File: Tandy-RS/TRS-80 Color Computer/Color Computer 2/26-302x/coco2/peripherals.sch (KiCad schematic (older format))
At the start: 45 parts, among them J1 Left Joystick, J2 Right Joystick, J3 RS232, J4 Cassette, J5 Conn_01x16_Female, K1 HB1-DC5V-H62, Q1 2N3055, U1 SC77527P, U2 6821, U3 SC77526, U7 6822

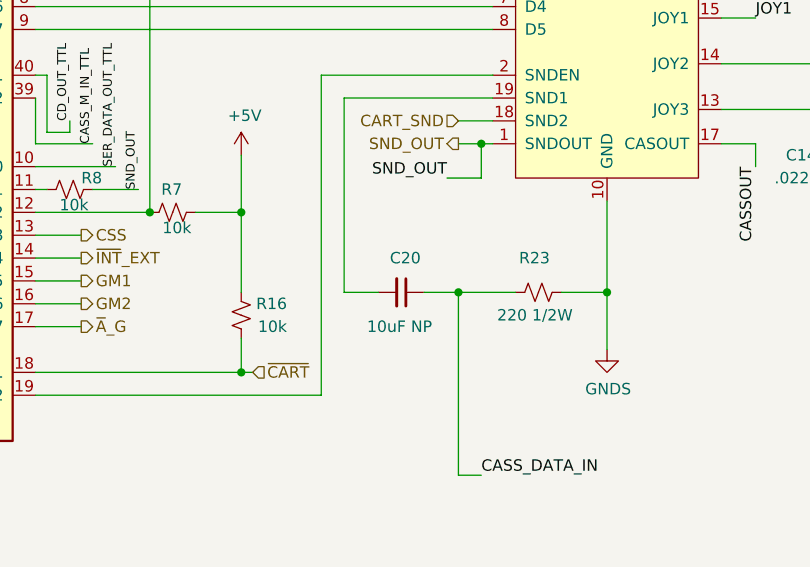
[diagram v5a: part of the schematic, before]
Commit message: Fixed some footprints that had wrong number of pins.
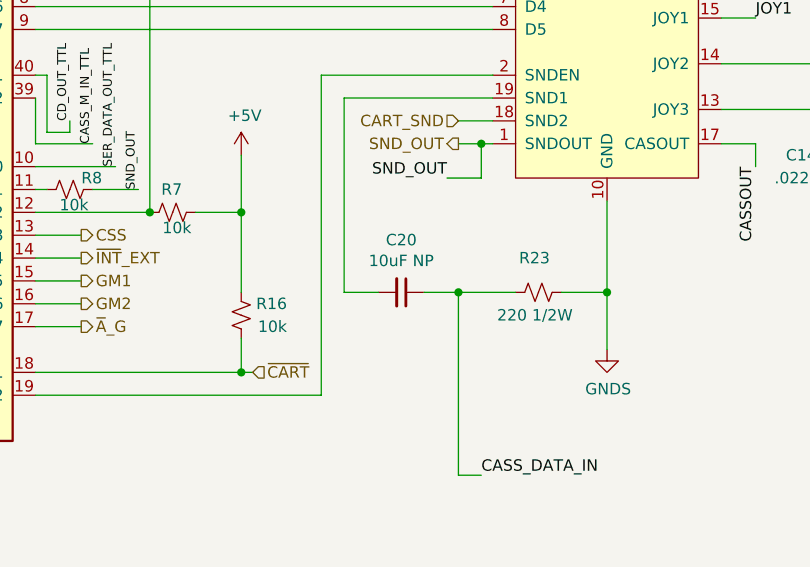
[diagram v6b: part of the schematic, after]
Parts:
- J5: footprint Connector_PinHeader_2.54mm:PinHeader_1x15_P2.54mm_Vertical -> Connector_PinHeader_2.54mm:PinHeader_1x16_P2.54mm_Vertical
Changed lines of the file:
@@
 F 0 "J5" H 5028 1826 50  0000 L CNN
 F 1 "Conn_01x16_Female" H 5028 1735 50  0000 L CNN
-F 2 "Connector_PinHeader_2.54mm:PinHeader_1x15_P2.54mm_Vertical" H 5000 1850 50  0001 C CNN
+F 2 "Connector_PinHeader_2.54mm:PinHeader_1x16_P2.54mm_Vertical" H 5000 1850 50  0001 C CNN
 F 3 "https://www.te.com/commerce/DocumentDelivery/DDEController?Action=srchrtrv&DocNm=520415&DocType=Customer+Drawing&DocLang=English" H 5000 1850 50  0001 C CNN
 F 4 "digikey" H 5000 1850 50  0001 C CNN "Vendor"
@@
 	5500 5900 5350 5900
 $Comp
-L Device:C_Small C20
-U 1 1 61067F63
-P 5100 6650
-F 0 "C20" V 4950 6600 50  0000 L CNN
-F 1 "10uF NP" V 5250 6500 50  0000 L CNN
-F 2 "Capacitor_THT:CP_Radial_D5.0mm_P2.50mm" H 5100 6650 50  0001 C CNN
-F 3 "http://nichicon-us.com/english/products/pdfs/e-ues.pdf" H 5100 6650 50  0001 C CNN
-F 4 "digikey" H 5100 6650 50  0001 C CNN "Vendor"
-F 5 "493-10824-1-ND" H 5100 6650 50  0001 C CNN "Vendor part#"
-F 6 "UES1E100MDM1TD" H 5100 6650 50  0001 C CNN "Manufacturer part#"
-	1    5100 6650
-	0    1    1    0
-$EndComp
-$Comp
 L Connector:DIN-4 J3
 U 1 1 61098034
@@
 Wire Wire Line
 	6300 550  6300 1850
+Connection ~ 10000 950
+$Comp
+L Device:C_Small C20
+U 1 1 605E886F
+P 5100 6650
+F 0 "C20" V 4871 6650 50  0000 C CNN
+F 1 "10uF NP" V 4962 6650 50  0000 C CNN
+F 2 "Capacitor_THT:CP_Radial_D5.0mm_P2.50mm" H 5100 6650 50  0001 C CNN
+F 3 "http://nichicon-us.com/english/products/pdfs/e-ues.pdf" H 5100 6650 50  0001 C CNN
+F 4 "digikey" V 5100 6650 50  0001 C CNN "Vendor"
+F 5 "493-10824-1-ND" V 5100 6650 50  0001 C CNN "Vendor part#"
+F 6 "UES1E100MDM1TD" V 5100 6650 50  0001 C CNN "Manufacturer part#"
+	1    5100 6650
+	0    1    1    0
+$EndComp
 Wire Bus Line
 	1000 1150 1000 5400
-Connection ~ 10000 950
 $EndSCHEMATC

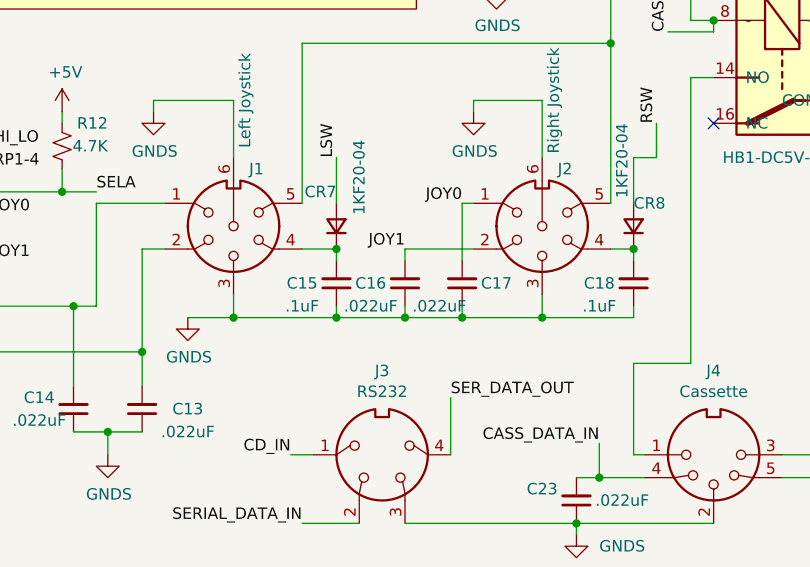
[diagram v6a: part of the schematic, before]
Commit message: -Finished PCB border -Placed components to match original board -added some 3D models for some components
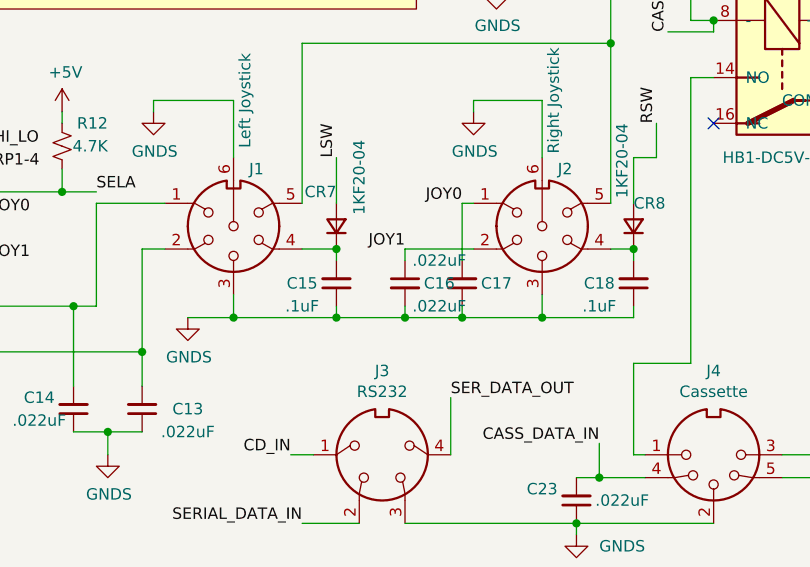
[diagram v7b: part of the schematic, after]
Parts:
- C13, C14, C16, C17, C22, C23: footprint Capacitor_THT:C_Disc_D8.0mm_W5.0mm_P5.00mm -> Capacitor_THT:C_Disc_D8.0mm_W2.5mm_P5.00mm
- C20: footprint Capacitor_THT:CP_Radial_D5.0mm_P2.50mm -> Capacitor_THT:C_Radial_D5.0mm_H11.0mm_P2.00mm
- CR7, CR8: footprint Diode_THT:D_DO-15_P15.24mm_Horizontal -> Diode_THT:D_A-405_P10.16mm_Horizontal
- R11, R23: footprint Resistor_THT:R_Axial_DIN0411_L9.9mm_D3.6mm_P20.32mm_Horizontal -> Resistor_THT:R_Axial_DIN0411_L9.9mm_D3.6mm_P12.70mm_Horizontal
- R2: footprint Resistor_THT:R_Axial_DIN0411_L9.9mm_D3.6mm_P20.32mm_Horizontal -> Resistor_THT:R_Axial_DIN0411_L9.9mm_D3.6mm_P15.24mm_Horizontal
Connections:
- net GNDS: now also C16.2; no longer C16.1
- net JOY1: now also C16.1; no longer C16.2
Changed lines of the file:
@@
 F 0 "R2" H 9332 2204 50  0000 R CNN
 F 1 ".1 ohms 1/2W" H 9332 2295 50  0000 R CNN
-F 2 "Resistor_THT:R_Axial_DIN0411_L9.9mm_D3.6mm_P20.32mm_Horizontal" H 9400 2250 50  0001 C CNN
+F 2 "Resistor_THT:R_Axial_DIN0411_L9.9mm_D3.6mm_P15.24mm_Horizontal" H 9400 2250 50  0001 C CNN
 F 3 "https://www.nteinc.com/resistor_web/pdf/halfw.pdf" H 9400 2250 50  0001 C CNN
 F 4 "digikey" H 9400 2250 50  0001 C CNN "Vendor"
@@
 F 0 "CR7" V 8300 5300 50  0000 L CNN
 F 1 "1KF20-04" H 8200 5200 50  0000 L CNN
-F 2 "Diode_THT:D_DO-15_P15.24mm_Horizontal" V 8150 5300 50  0001 C CNN
+F 2 "Diode_THT:D_A-405_P10.16mm_Horizontal" V 8150 5300 50  0001 C CNN
 F 3 "https://www.nteinc.com/specs/100to199/pdf/nte109.pdf" V 8150 5300 50  0001 C CNN
 F 4 "digikey" H 8150 5300 50  0001 C CNN "Vendor"
@@
 F 0 "CR8" V 9550 5300 50  0000 R CNN
 F 1 "1KF20-04" H 9900 5350 50  0000 R CNN
-F 2 "Diode_THT:D_DO-15_P15.24mm_Horizontal" V 9450 5300 50  0001 C CNN
+F 2 "Diode_THT:D_A-405_P10.16mm_Horizontal" V 9450 5300 50  0001 C CNN
 F 3 "https://www.nteinc.com/specs/100to199/pdf/nte109.pdf" V 9450 5300 50  0001 C CNN
 F 4 "digikey" H 9450 5300 50  0001 C CNN "Vendor"
@@
 F 0 "C13" H 7100 6100 50  0000 C CNN
 F 1 ".022uF" H 7100 6200 50  0000 C CNN
-F 2 "Capacitor_THT:C_Disc_D8.0mm_W5.0mm_P5.00mm" H 7300 6100 50  0001 C CNN
+F 2 "Capacitor_THT:C_Disc_D8.0mm_W2.5mm_P5.00mm" H 7300 6100 50  0001 C CNN
 F 3 "https://www.nteinc.com/capacitor_web/pdf/89000.pdf" H 7300 6100 50  0001 C CNN
 F 4 "digikey" H 7300 6100 50  0001 C CNN "Vendor"
@@
 F 6 "89322" H 7300 6100 50  0001 C CNN "Manufacturer part#"
 	1    7300 6100
-	-1   0    0    1
-$EndComp
-$Comp
-L Device:C_Small C?
-U 1 1 611BFE42
-P 7000 6100
-AR Path="/602A51A8/611BFE42" Ref="C?"  Part="1"
-AR Path="/603CF7B8/611BFE42" Ref="C14"  Part="1"
-F 0 "C14" H 7150 6050 50  0000 C CNN
-F 1 ".022uF" H 7150 6150 50  0000 C CNN
-F 2 "Capacitor_THT:C_Disc_D8.0mm_W5.0mm_P5.00mm" H 7000 6100 50  0001 C CNN
-F 3 "https://www.nteinc.com/capacitor_web/pdf/89000.pdf" H 7000 6100 50  0001 C CNN
-F 4 "digikey" H 7000 6100 50  0001 C CNN "Vendor"
-F 5 "2368-89322-ND" H 7000 6100 50  0001 C CNN "Vendor part#"
-F 6 "89322" H 7000 6100 50  0001 C CNN "Manufacturer part#"
-	1    7000 6100
 	-1   0    0    1
 $EndComp
@@
 F 0 "C16" H 8600 5550 50  0000 C CNN
 F 1 ".022uF" H 8600 5650 50  0000 C CNN
-F 2 "Capacitor_THT:C_Disc_D8.0mm_W5.0mm_P5.00mm" H 8450 5550 50  0001 C CNN
+F 2 "Capacitor_THT:C_Disc_D8.0mm_W2.5mm_P5.00mm" H 8450 5550 50  0001 C CNN
 F 3 "https://www.nteinc.com/capacitor_web/pdf/89000.pdf" H 8450 5550 50  0001 C CNN
 F 4 "digikey" H 8450 5550 50  0001 C CNN "Vendor"
@@
 F 6 "89322" H 8450 5550 50  0001 C CNN "Manufacturer part#"
 	1    8450 5550
-	-1   0    0    1
+	1    0    0    -1
 $EndComp
 $Comp
@@
 F 0 "C17" H 8550 5550 50  0000 C CNN
 F 1 ".022uF" H 8800 5650 50  0000 C CNN
-F 2 "Capacitor_THT:C_Disc_D8.0mm_W5.0mm_P5.00mm" H 8700 5550 50  0001 C CNN
+F 2 "Capacitor_THT:C_Disc_D8.0mm_W2.5mm_P5.00mm" H 8700 5550 50  0001 C CNN
 F 3 "https://www.nteinc.com/capacitor_web/pdf/89000.pdf" H 8700 5550 50  0001 C CNN
 F 4 "digikey" H 8700 5550 50  0001 C CNN "Vendor"
@@
 F 0 "C23" H 9350 6450 50  0000 C CNN
 F 1 ".022uF" H 9000 6500 50  0000 C CNN
-F 2 "Capacitor_THT:C_Disc_D8.0mm_W5.0mm_P5.00mm" H 9200 6500 50  0001 C CNN
+F 2 "Capacitor_THT:C_Disc_D8.0mm_W2.5mm_P5.00mm" H 9200 6500 50  0001 C CNN
 F 3 "https://www.nteinc.com/capacitor_web/pdf/89000.pdf" H 9200 6500 50  0001 C CNN
 F 4 "digikey" H 9200 6500 50  0001 C CNN "Vendor"
@@
 F 0 "C22" V 8721 4150 50  0000 C CNN
 F 1 ".022uF" V 8812 4150 50  0000 C CNN
-F 2 "Capacitor_THT:C_Disc_D8.0mm_W5.0mm_P5.00mm" H 8950 4150 50  0001 C CNN
+F 2 "Capacitor_THT:C_Disc_D8.0mm_W2.5mm_P5.00mm" H 8950 4150 50  0001 C CNN
 F 3 "https://www.nteinc.com/capacitor_web/pdf/89000.pdf" H 8950 4150 50  0001 C CNN
 F 4 "digikey" H 8950 4150 50  0001 C CNN "Vendor"
@@
 F 0 "R11" H 9300 3850 50  0000 R CNN
 F 1 "100 1/2W" H 9750 3950 50  0000 R CNN
-F 2 "Resistor_THT:R_Axial_DIN0411_L9.9mm_D3.6mm_P20.32mm_Horizontal" H 9350 3850 50  0001 C CNN
+F 2 "Resistor_THT:R_Axial_DIN0411_L9.9mm_D3.6mm_P12.70mm_Horizontal" H 9350 3850 50  0001 C CNN
 F 3 "https://www.seielect.com/catalog/sei-cf_cfm.pdf" H 9350 3850 50  0001 C CNN
 F 4 "digikey" H 9350 3850 50  0001 C CNN "Vendor"
@@
 F 0 "R23" V 5550 6700 50  0000 R CNN
 F 1 "220 1/2W" V 5800 6800 50  0000 R CNN
-F 2 "Resistor_THT:R_Axial_DIN0411_L9.9mm_D3.6mm_P20.32mm_Horizontal" H 5700 6650 50  0001 C CNN
+F 2 "Resistor_THT:R_Axial_DIN0411_L9.9mm_D3.6mm_P12.70mm_Horizontal" H 5700 6650 50  0001 C CNN
 F 3 "https://www.seielect.com/catalog/sei-cf_cfm.pdf" H 5700 6650 50  0001 C CNN
 F 4 "digikey" H 5700 6650 50  0001 C CNN "Vendor"
@@
 F 0 "C20" V 4871 6650 50  0000 C CNN
 F 1 "10uF NP" V 4962 6650 50  0000 C CNN
-F 2 "Capacitor_THT:CP_Radial_D5.0mm_P2.50mm" H 5100 6650 50  0001 C CNN
+F 2 "Capacitor_THT:C_Radial_D5.0mm_H11.0mm_P2.00mm" H 5100 6650 50  0001 C CNN
 F 3 "http://nichicon-us.com/english/products/pdfs/e-ues.pdf" H 5100 6650 50  0001 C CNN
 F 4 "digikey" V 5100 6650 50  0001 C CNN "Vendor"
@@
 Wire Bus Line
 	1000 1150 1000 5400
+$Comp
+L Device:C_Small C?
+U 1 1 611BFE42
+P 7000 6100
+AR Path="/602A51A8/611BFE42" Ref="C?"  Part="1"
+AR Path="/603CF7B8/611BFE42" Ref="C14"  Part="1"
+F 0 "C14" H 7150 6050 50  0000 C CNN
+F 1 ".022uF" H 7150 6150 50  0000 C CNN
+F 2 "Capacitor_THT:C_Disc_D8.0mm_W2.5mm_P5.00mm" H 7000 6100 50  0001 C CNN
+F 3 "https://www.nteinc.com/capacitor_web/pdf/89000.pdf" H 7000 6100 50  0001 C CNN
+F 4 "digikey" H 7000 6100 50  0001 C CNN "Vendor"
+F 5 "2368-89322-ND" H 7000 6100 50  0001 C CNN "Vendor part#"
+F 6 "89322" H 7000 6100 50  0001 C CNN "Manufacturer part#"
+	1    7000 6100
+	-1   0    0    1
+$EndComp
 $EndSCHEMATC

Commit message: -Added more 3 models. -Improved alignment on some of the components.
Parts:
- Q1: Description 2nd part (none) -> Heatsink; Manufacturer 2nd part# (none) -> 501603B00000G; Vendor 2nd part# (none) -> HS110-ND
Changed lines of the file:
@@
 F 5 "2383-2N3055-ND" H 9300 1850 50  0001 C CNN "Vendor part#"
 F 6 "2N3055" H 9300 1850 50  0001 C CNN "Manufacturer part#"
+F 7 "Heatsink" H 9300 1850 50  0001 C CNN "Description 2nd part"
+F 8 "HS110-ND" H 9300 1850 50  0001 C CNN "Vendor 2nd part#"
+F 9 "501603B00000G" H 9300 1850 50  0001 C CNN "Manufacturer 2nd part#"
 	1    9300 1850
 	1    0    0    -1
@@
 	0    1    1    0
 $EndComp
-Wire Bus Line
-	1000 1150 1000 5400
 $Comp
 L Device:C_Small C?
@@
 	-1   0    0    1
 $EndComp
+Wire Bus Line
+	1000 1150 1000 5400
 $EndSCHEMATC
